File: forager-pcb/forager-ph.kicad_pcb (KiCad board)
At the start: 2 copper layers, 114.6 x 96.3 mm, 26 parts

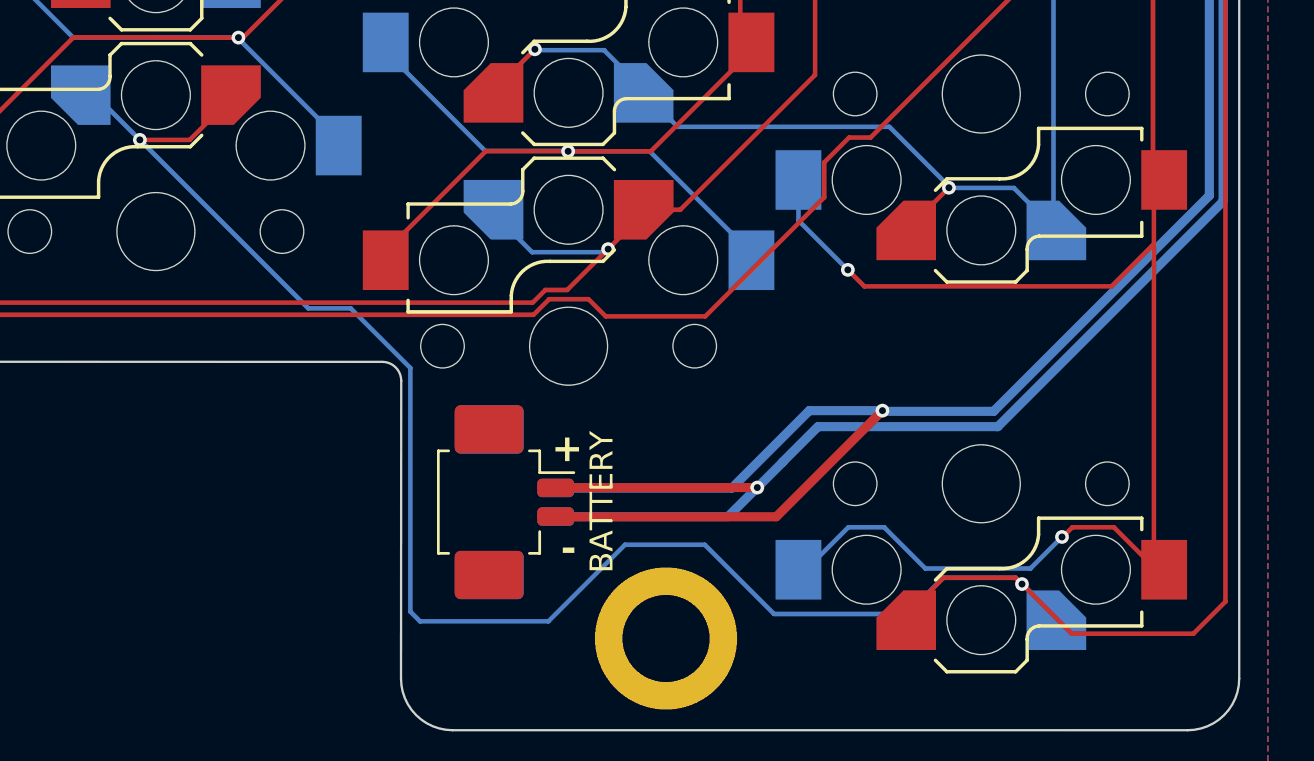
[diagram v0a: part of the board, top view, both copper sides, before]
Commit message: Rotate battery connection and move back to give clearance,
Beware the bottom case ribs...
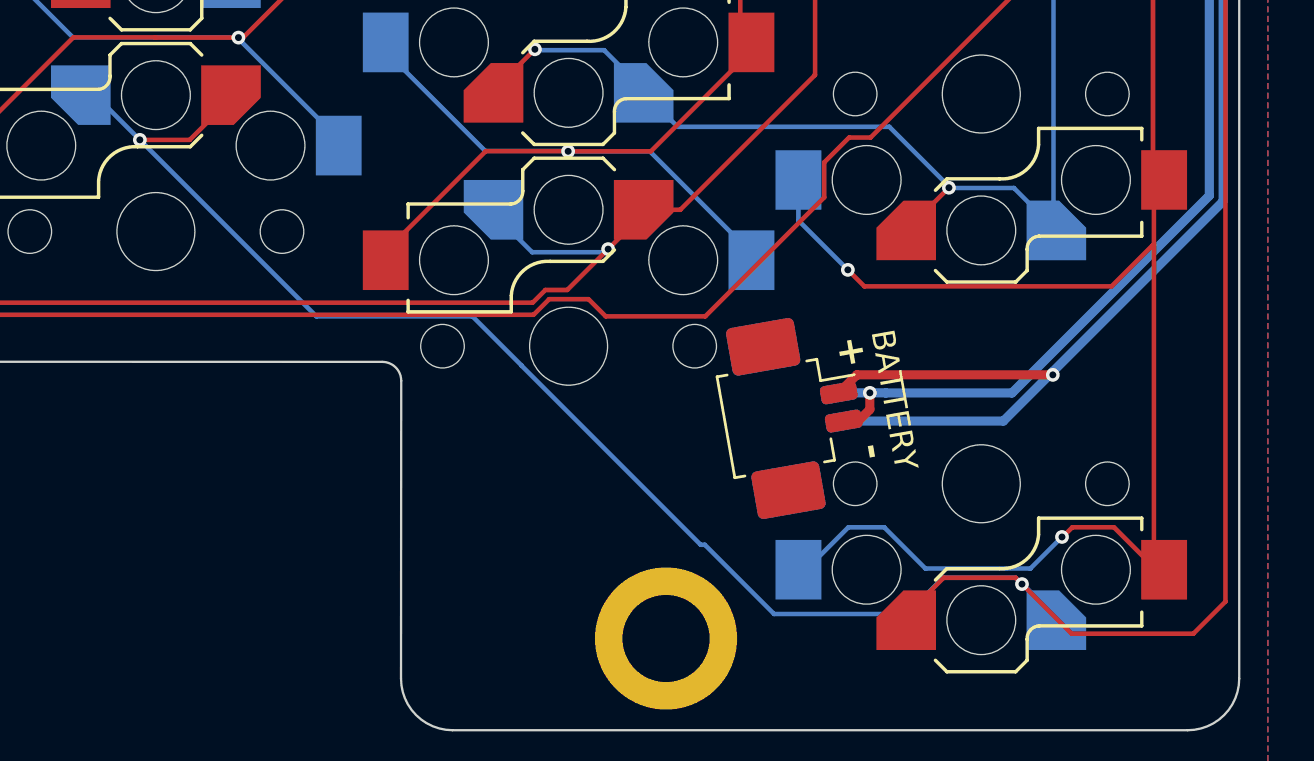
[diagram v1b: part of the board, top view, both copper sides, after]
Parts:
- moved BATTERY 13.0 mm to (98.5, 3.07), turned to -80 degrees
- moved BAT 13.0 mm to (98.5, 3.07), turned to 100 degrees
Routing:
- net GND: track 143.4 -> 114.0 mm
- net BAT: track 96.4 -> 81.8 mm
- net R4: track 148.0 -> 139.0 mm
